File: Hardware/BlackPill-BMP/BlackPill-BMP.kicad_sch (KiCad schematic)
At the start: 39 parts, among them J1 JTAG, J2 VCC, J3 GND, J4 SWO, J5 GDB_COMM, J6 TVCC, J7 LogicAna, J8 Conn_01x10, J9 Conn_01x11, U1 BlueAndBlackPill, U2 AD8531ARTZ, U3 SRV05-4, U4 TXS0108EPW, U5 SRV05-4

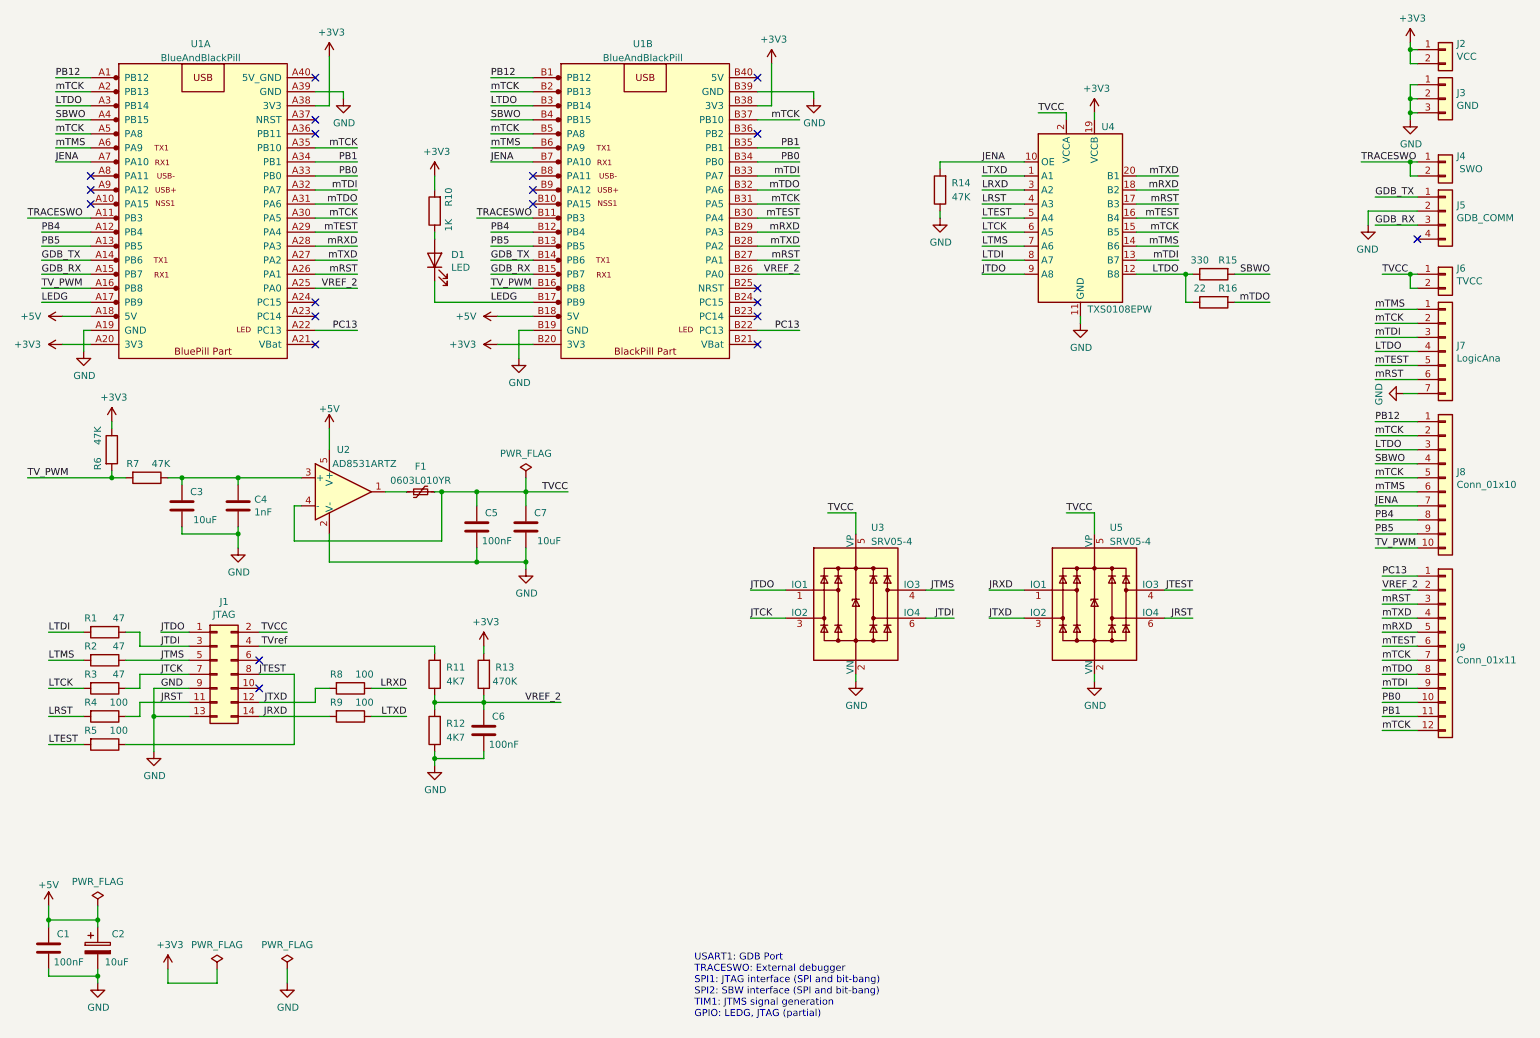
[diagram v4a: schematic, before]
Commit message: Swapped LRXD and LTXD on both prototype boards.
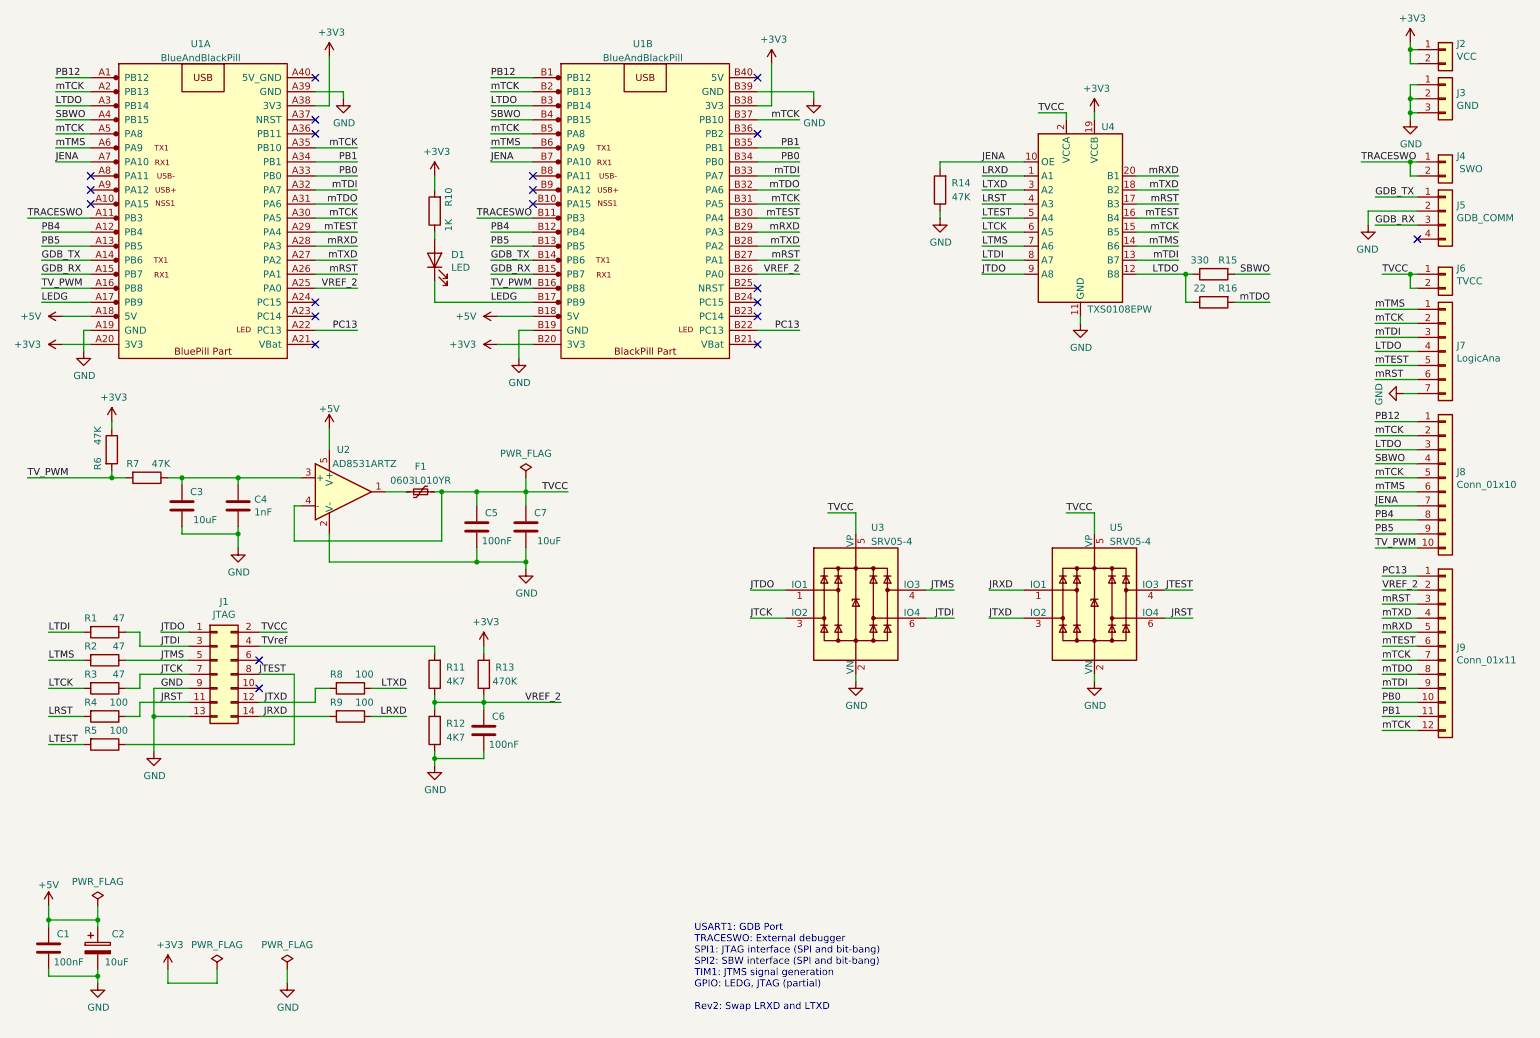
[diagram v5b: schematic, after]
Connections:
- net LRXD: now also R9.1, U4.1 (A1); no longer R8.1, U4.3 (A2)
- net LTXD: now also R8.1, U4.3 (A2); no longer R9.1, U4.1 (A1)
- net mRXD: now also U4.20 (B1); no longer U4.18 (B2)
- net mTXD: now also U4.18 (B2); no longer U4.20 (B1)
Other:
- note added: "USART1: GDB Port TRACESWO: External debugger SPI1: JTAG interface (SPI and bit-bang) SPI2: SBW interface (SPI and bit-bang) TIM1: JTMS signal generation GPIO: LEDG, JTAG (partial) Rev2: Swap LRXD and LTXD"
- note removed: "USART1: GDB Port TRACESWO: External debugger SPI1: JTAG interface (SPI and bit-bang) SPI2: SBW interface (SPI and bit-bang) TIM1: JTMS signal generation GPIO: LEDG, JTAG (partial)"
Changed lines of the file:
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@@
   (title_block
     (title "MSPBMP Development Protoboard")
-    (date "2022-08-02")
-    (rev "1")
+    (date "2022-08-18")
+    (rev "2")
     (company "Mathias Gruber")
     (comment 1 "BluePill and BlackPill option")
@@
     (stroke (width 0) (type default) (color 0 0 0 0))
   )
-  (text "USART1: GDB Port\nTRACESWO: External debugger\nSPI1: JTAG interface (SPI and bit-bang)\nSPI2: SBW interface (SPI and bit-bang)\nTIM1: JTMS signal generation\nGPIO: LEDG, JTAG (partial)"
-    (at 135.89 195.58 0)
+  (text "USART1: GDB Port\nTRACESWO: External debugger\nSPI1: JTAG interface (SPI and bit-bang)\nSPI2: SBW interface (SPI and bit-bang)\nTIM1: JTMS signal generation\nGPIO: LEDG, JTAG (partial)\n\nRev2: Swap LRXD and LTXD"
+    (at 135.89 194.31 0)
     (effects (font (size 1.27 1.27)) (justify left bottom))
   )
@@
     (effects (font (size 1.27 1.27)) (justify left bottom))
   )
-  (label "LRXD" (at 83.82 135.89 180)
+  (label "LRXD" (at 83.82 140.97 180)
     (effects (font (size 1.27 1.27)) (justify right bottom))
   )
@@
     (effects (font (size 1.27 1.27)) (justify left bottom))
   )
-  (label "mTXD" (at 223.52 43.18 180)
+  (label "mTXD" (at 223.52 45.72 180)
     (effects (font (size 1.27 1.27)) (justify right bottom))
   )
@@
     (effects (font (size 1.27 1.27)) (justify right bottom))
   )
-  (label "LTXD" (at 187.96 43.18 0)
+  (label "LTXD" (at 187.96 45.72 0)
     (effects (font (size 1.27 1.27)) (justify left bottom))
   )
@@
     (effects (font (size 1.27 1.27)) (justify left bottom))
   )
-  (label "LTXD" (at 83.82 140.97 180)
+  (label "LTXD" (at 83.82 135.89 180)
     (effects (font (size 1.27 1.27)) (justify right bottom))
   )
@@
     (effects (font (size 1.27 1.27)) (justify left bottom))
   )
-  (label "mRXD" (at 223.52 45.72 180)
+  (label "mRXD" (at 223.52 43.18 180)
     (effects (font (size 1.27 1.27)) (justify right bottom))
   )
@@
     (effects (font (size 1.27 1.27)) (justify left bottom))
   )
-  (label "LRXD" (at 187.96 45.72 0)
-    (effects (font (size 1.27 1.27)) (justify left bottom))
-  )
+  (label "LRXD" (at 187.96 43.18 0)
+    (effects (font (size 1.27 1.27)) (justify left bottom))
+  )
